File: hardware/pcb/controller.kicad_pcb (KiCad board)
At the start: 2 copper layers, 100 x 75 mm, 18 parts, among them J1 TerminalBlock_MaiXu_MX126-5.0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, J2 TerminalBlock_MaiXu_MX126-5.0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, J3 TerminalBlock_MaiXu_MX126-5.0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, J4 TerminalBlock_MaiXu_MX126-5.0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, J5 TerminalBlock_MaiXu_MX126-5.0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, U1L PinSocket_1x15_P2.54mm_Vertic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, U1R PinSocket_1x15_P2.54mm_Vertic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

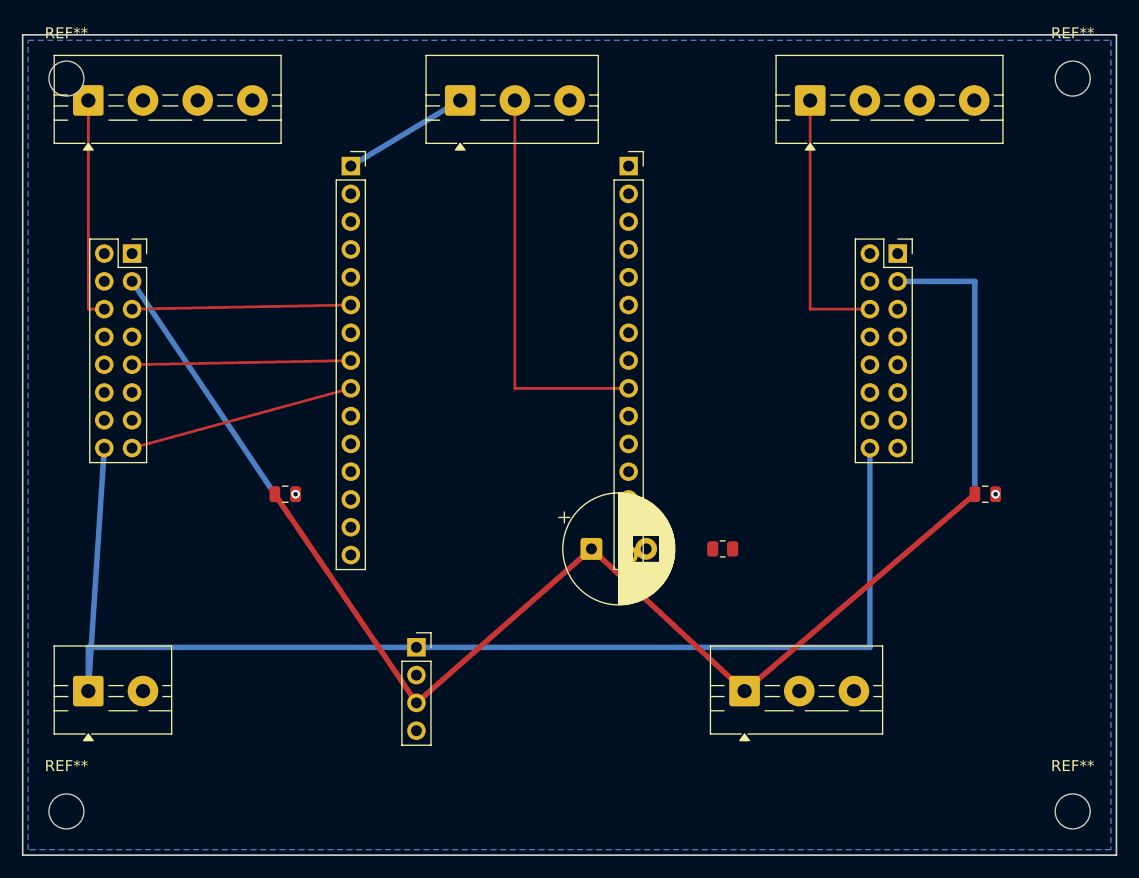
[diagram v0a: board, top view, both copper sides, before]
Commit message: Freerouting: kalan sinyaller tamamlandi -> TAM ROUTING (ratsnest=0)
- Java 25 (Temurin) + Freerouting 2.2.4 ile headless autoroute
- pcbnew DSN export headless'ta calismiyor -> make_dsn.py geometriden DSN uretir
  (GND = B.Cu plane), build_kicad.py SES_FILE modu SES'i parse edip uygular
- freeroute.sh: make_dsn -> Freerouting -> SES uygula -> kicad_export zinciri
- 23 sinyal neti tam routlu (139 iz + 3 via); GND plane yeni geometriye gore
  yeniden self-fill'lendi
- DRC: ratsnest=0, short=0, bakir clearance=0 (zone clearance kurali duzeltildi);
  kalan 148 ihlal kozmetik (129 kutuphane silk + ~12 plane artefakti)
- final/ Gerber + STEP + PDF + DRC yenilendi; F_Cu/B_Cu render'lari eklendi
- apply_ses.py kaldirildi (build_kicad SES moduna entegre)

Co-Authored-By: Claude Opus 4.8 <noreply@anthropic.com>
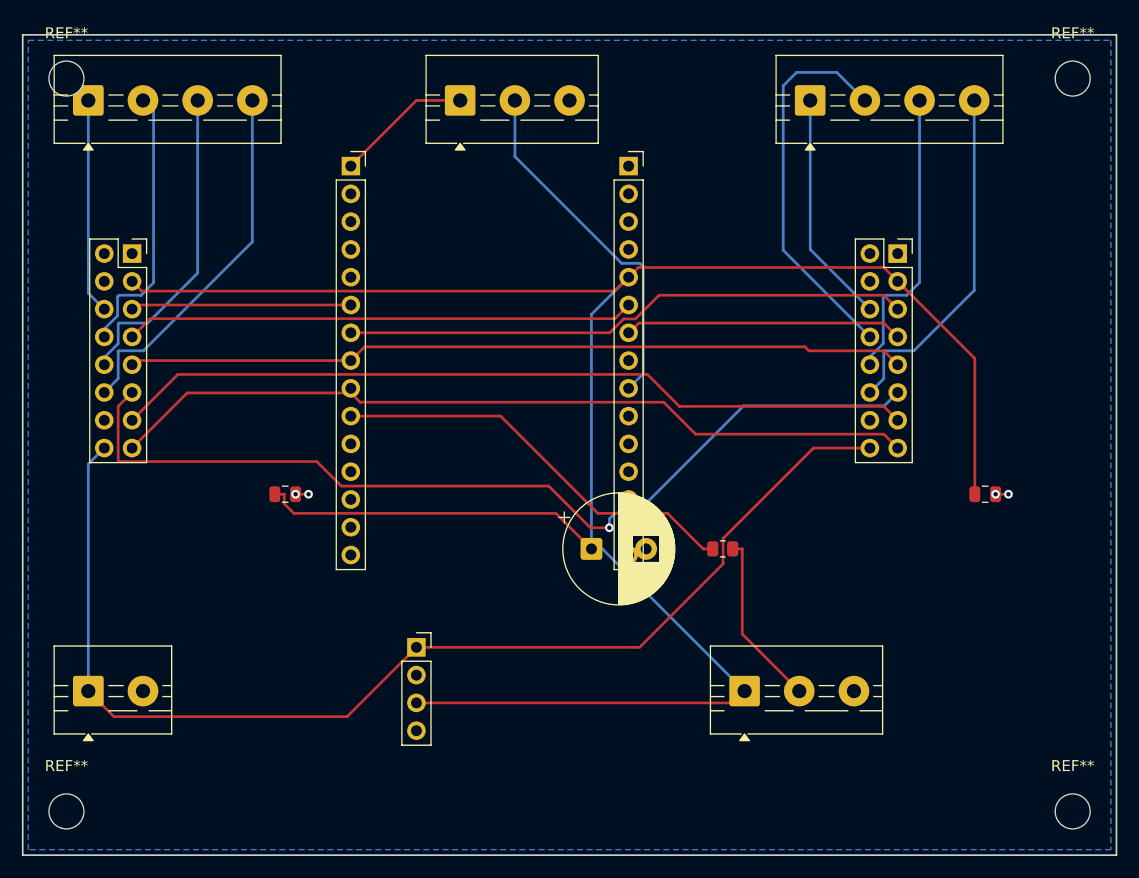
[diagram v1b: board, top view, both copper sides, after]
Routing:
- net N_MS2: track 0.00 -> 86.2 mm, vias 0 -> 1
- net N_MS1: track 0.00 -> 73.5 mm
- net N_5V: track 141.1 -> 201.8 mm
- net N_EN: track 20.7 -> 74.6 mm
- net N_RHDIR: track 0.00 -> 51.9 mm
- net N_UART: track 20.0 -> 71.4 mm
- net N_THSTEP: track 0.00 -> 46.6 mm
- net N_LEDG: track 0.00 -> 38.1 mm
- net RHM_A2: track 0.00 -> 35.3 mm
- net THM_B2: track 0.00 -> 33.6 mm
- net RHM_B2: track 0.00 -> 32.2 mm
- net THM_B1: track 0.00 -> 29.2 mm
- net RHM_B1: track 0.00 -> 27.2 mm
- net N_RHSTEP: track 0.00 -> 25.5 mm
- net THM_A2: track 0.00 -> 25.1 mm
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
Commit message: PCB Rev-B: inceleme bulgulari islendi + yeniden route (bastirilabilir)
build_kicad.py Rev-B eklemeleri:
- TMC2209 UART adres cakismasi -> A1=adr0 (MS1/MS2=GND), A2=adr1 (MS1=5V); ayri adres
- WS2812 level shifter U2 (74AHCT1G125 SOT-23-5): GPIO4 3.3V -> 5V DIN; R1 cikis serisi
- 12V giris korumasi: F1 sigorta + Q1 P-FET ters polarite + D1 zener + R2 gate
- TMC VM: C6 100uF bulk + C7/C8 100nF decap
- EN boot pasif: R3 10k pull-up (EN->VIO)
- UART half-duplex: R4 1k (TX->PDN), RX PDN'e taps
-> Freerouting tam route: 196 iz + 12 via, DRC 0 short / 0 ratsnest / 0 bakir clearance
   yeni Gerber + STEP + DRC uretildi (final/)

DURUM: Rev-B tasarimi dondurdu; HALA fiziksel uretilmedi/test edilmedi.
PCB_inceleme.md + URETIM_DOSYASI.md + muhendislik.html guncellendi.

Co-Authored-By: Claude Opus 4.8 <noreply@anthropic.com>
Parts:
- added C5: C_0805_2012Metric, C_0805_2012Metric, F.Cu at (84.0, 52.0)
- added C6: CP_Radial_D8.0mm_P3.50mm, CP_Radial_D8.0mm_P3.50mm, F.Cu at (46.0, 67.0)
- added C7: C_0805_2012Metric, C_0805_2012Metric, F.Cu at (18.0, 34.0)
- added C8: C_0805_2012Metric, C_0805_2012Metric, F.Cu at (72.0, 34.0)
- added D1: D_SOD-323, D_SOD-323, F.Cu at (30.0, 68.0)
- added F1: Fuse_1206_3216Metric, Fuse_1206_3216Metric, F.Cu at (16.0, 66.0)
- added Q1: SOT-23, SOT-23, F.Cu at (24.0, 66.0)
- added R2: R_0805_2012Metric, R_0805_2012Metric, F.Cu at (30.0, 64.0)
- added R3: R_0805_2012Metric, R_0805_2012Metric, F.Cu at (60.0, 66.0)
- added R4: R_0805_2012Metric, R_0805_2012Metric, F.Cu at (52.0, 64.0)
- added U2: SOT-23-5, SOT-23-5, F.Cu at (78.0, 50.0)
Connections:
- A1 pad 11: N_MS2 -> N_GND
- A1 pad 13: N_MS1 -> N_GND
- A1 pad 9: N_UART -> N_PDN
- A2 pad 11: N_MS2 -> N_GND
- A2 pad 13: N_MS1 -> N_5V
- A2 pad 9: N_UART -> N_PDN
- J1 pad 1: N_12V -> N_12VIN
- R1 pad 1: N_LEDG -> N_LEDDIN5
- U1L pad 8: N_UART -> N_UART_TX
- U1R pad 8: N_UART_RX -> N_PDN
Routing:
- net N_PDN: track 0.00 -> 111.9 mm, vias 0 -> 1
- net N_MS2: track 86.2 -> 0.00 mm, vias 1 -> 0
- net N_MS1: track 73.5 -> 0.00 mm
- net N_UART: track 71.4 -> 0.00 mm
- net N_UART_TX: track 0.00 -> 52.9 mm, vias 0 -> 1
- net N_EN: track 74.6 -> 116.0 mm, vias 0 -> 1
- net N_12V: track 106.8 -> 140.4 mm
- net N_5V: track 201.8 -> 229.1 mm
- net N_LEDDIN5: track 0.00 -> 20.0 mm
- net N_LEDG: track 38.1 -> 53.1 mm
- net N_12VIN: track 0.00 -> 11.1 mm
- net N_PGATE: track 0.00 -> 10.8 mm
- net N_GND: track 2.36 -> 10.9 mm, vias 4 -> 16
- net N_12VF: track 0.00 -> 7.54 mm
- net RHM_B2: track 32.2 -> 39.7 mm
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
